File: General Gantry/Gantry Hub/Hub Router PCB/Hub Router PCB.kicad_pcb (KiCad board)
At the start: 4 copper layers, 140 x 85 mm, 14 parts, among them J1 178-025-513R571, J2 178-037-513R571, J3 Barrel_Jack, J4 Barrel_Jack, J5 Barrel_Jack, J6 Barrel_Jack, J7 Conn_01x02

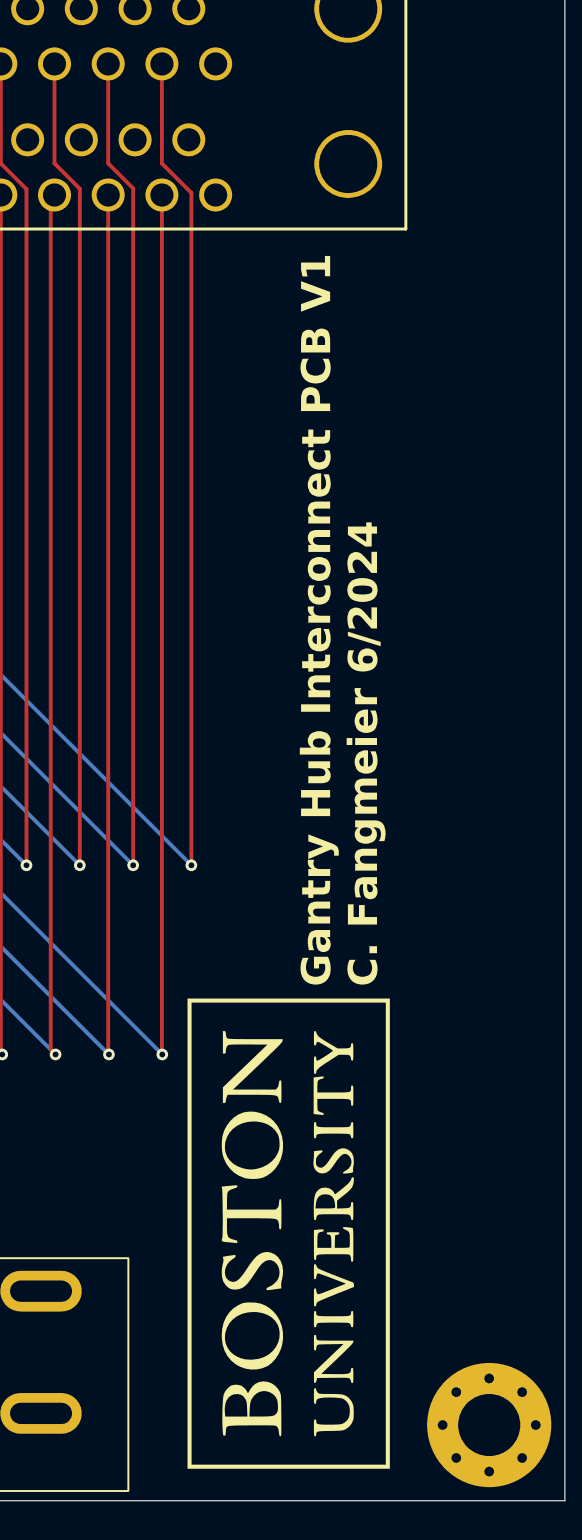
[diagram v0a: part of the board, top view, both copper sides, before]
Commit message: Updates to gantry hub box
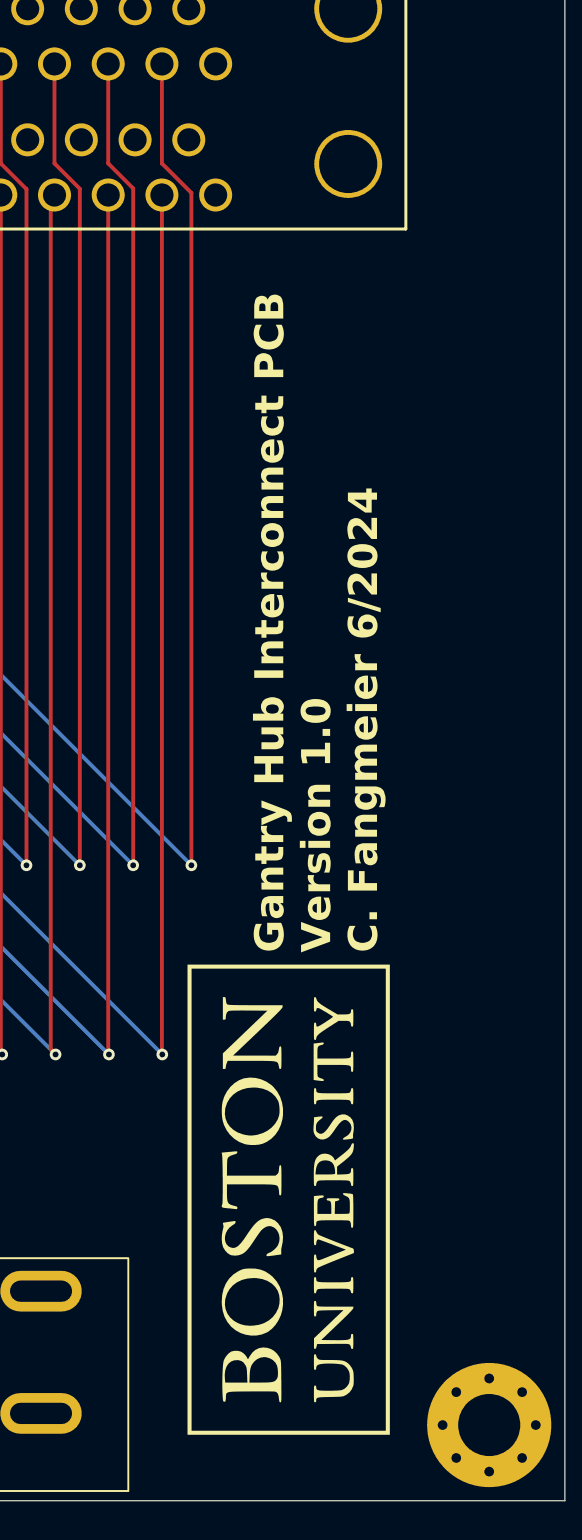
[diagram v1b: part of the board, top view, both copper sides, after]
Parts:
- moved G*** 1.75 mm to (172.8, 117.0)
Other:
- board text added: "Gantry Hub Interconnect PCB Version 1.0 C. Fangmeier 6/2024"
- board text removed: "Gantry Hub Interconnect PCB V1 C. Fangmeier 6/2024"
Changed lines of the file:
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@@
 	(footprint "LOGO"
 		(layer "F.Cu")
-		(at 172.75 118.75 90)
+		(at 172.75 117 90)
 		(property "Reference" "G***"
-			(at 0 0 270)
+			(at 0 0 -90)
 			(layer "Dwgs.User")
 			(effects
@@
 		)
 		(property "Value" "LOGO"
-			(at 0.75 0 270)
+			(at 0.75 0 -90)
 			(layer "F.SilkS")
 			(hide yes)
@@
 		)
 	)
-	(gr_text "Gantry Hub Interconnect PCB V1\nC. Fangmeier 6/2024"
-		(at 177.5 106 90)
+	(gr_text "Gantry Hub Interconnect PCB\nVersion 1.0\nC. Fangmeier 6/2024"
+		(at 177.5 104.25 90)
 		(layer "F.SilkS")
 		(effects
